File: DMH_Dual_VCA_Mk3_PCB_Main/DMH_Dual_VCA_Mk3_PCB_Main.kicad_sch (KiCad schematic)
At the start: 58 parts, among them J1 TRS_Jack_6.35mm_Sw, J10 IDC_02x05, J11 Conn_01x06, J12 Conn_01x08, J13 Conn_01x06, J14 Conn_01x06, J15 Conn_01x08, J16 Conn_01x06, J17 IDC_02x05, J18 Conn_02x03_Odd_Even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

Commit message: Schematic redesign done
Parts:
- J20, JP1: now in the parts list

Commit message: Controls PCB comp placement started
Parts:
- J12: footprint Connector_PinSocket_2.54mm:PinSocket_1x06_P2.54mm_Vertical -> Connector_PinSocket_2.54mm:PinSocket_1x08_P2.54mm_Vertical
- J15: footprint Connector_PinHeader_2.54mm:PinHeader_1x06_P2.54mm_Vertical -> Connector_PinHeader_2.54mm:PinHeader_1x08_P2.54mm_Vertical
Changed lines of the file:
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@@
 			)
 		)
-		(property "Footprint" "Connector_PinSocket_2.54mm:PinSocket_1x06_P2.54mm_Vertical"
+		(property "Footprint" "Connector_PinSocket_2.54mm:PinSocket_1x08_P2.54mm_Vertical"
 			(at 101.6 195.58 0)
 			(hide yes)
@@
 			(at 101.6 195.58 0)
 			(hide yes)
+			(show_name no)
+			(do_not_autoplace no)
+			(effects
+				(font
+					(size 1.27 1.27)
+				)
+			)
+		)
+		(property "Function" ""
+			(at 101.6 195.58 0)
 			(show_name no)
 			(do_not_autoplace no)
@@
 			)
 		)
-		(property "Footprint" "Connector_PinHeader_2.54mm:PinHeader_1x06_P2.54mm_Vertical"
+		(property "Footprint" "Connector_PinHeader_2.54mm:PinHeader_1x08_P2.54mm_Vertical"
 			(at 139.7 195.58 0)
 			(hide yes)
@@
 			(show_name no)
 			(do_not_autoplace no)
+			(effects
+				(font
+					(size 1.27 1.27)
+				)
+			)
+		)
+		(property "Function" ""
+			(at 139.7 195.58 0)
+			(show_name no)
+			(do_not_autoplace no)

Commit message: Started Main PCB comp placement
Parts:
- removed J21: Conn_01x04, Connector_PinHeader_2.54mm:PinHeader_1x04_P2.54mm_Vertical, symbol Connector_Generic:Conn_01x04
- removed J24: Conn_01x04, Connector_PinSocket_2.54mm:PinSocket_1x04_P2.54mm_Vertical, symbol Connector_Generic:Conn_01x04
- J11: footprint Connector_PinSocket_2.54mm:PinSocket_1x06_P2.54mm_Vertical -> Connector_PinHeader_2.54mm:PinHeader_1x06_P2.54mm_Vertical
- J12: footprint Connector_PinSocket_2.54mm:PinSocket_1x08_P2.54mm_Vertical -> Connector_PinHeader_2.54mm:PinHeader_1x08_P2.54mm_Vertical
- J14, J16: footprint Connector_PinHeader_2.54mm:PinHeader_1x06_P2.54mm_Vertical -> Connector_PinSocket_2.54mm:PinSocket_1x06_P2.54mm_Vertical
- J15: footprint Connector_PinHeader_2.54mm:PinHeader_1x08_P2.54mm_Vertical -> Connector_PinSocket_2.54mm:PinSocket_1x08_P2.54mm_Vertical
- J18, J19, J22, J23: footprint Connector_PinHeader_2.54mm:PinHeader_2x03_P2.54mm_Horizontal -> Connector_PinSocket_2.54mm:PinSocket_2x03_P2.54mm_Vertical
- J20: now left out of the parts list
- JP1: footprint (none) -> Connector_PinHeader_2.54mm:PinHeader_1x03_P2.54mm_Vertical; now left out of the parts list
- U4: footprint (none) -> Package_DIP:DIP-8_W7.62mm_Socket
- renumbered J17 to J100, J10 to J200
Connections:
- net +12V: now also J13.5 (Pin_5), J16.5 (Pin_5); no longer J13.2 (Pin_2), J16.2 (Pin_2)
- net +5V: now also J13.2 (Pin_2), J16.2 (Pin_2); no longer J13.4 (Pin_4), J16.4 (Pin_4)
- net -12V: now also J13.4 (Pin_4), J16.4 (Pin_4); no longer J13.3 (Pin_3), J16.3 (Pin_3)
- net -5V: now also J13.3 (Pin_3), J16.3 (Pin_3); no longer J13.5 (Pin_5), J16.5 (Pin_5)
- net Attenuverted_CV_PT_c: now also J15.4 (Pin_4); no longer J15.3 (Pin_3)
- net Attenuverted_CV_PT_m: now also J12.4 (Pin_4); no longer J12.3 (Pin_3)
- net Balanced_Offset_c: now also J15.6 (Pin_6); no longer J15.1 (Pin_1)
- net Balanced_Offset_m: now also J12.6 (Pin_6); no longer J12.1 (Pin_1)
- net CV_In_A2_N_m: now also J200.6 (Pin_6); no longer J200.4 (Pin_4)
- net CV_In_B2_N_m: now also J200.8 (Pin_8); no longer J200.6 (Pin_6)
- net CV_In_PT_c: now also J15.1 (Pin_1); no longer J15.8 (Pin_8)
- net CV_In_PT_m: now also J12.1 (Pin_1); no longer J12.8 (Pin_8)
- net CV_PT_Offset_c: now also J15.8 (Pin_8); no longer J15.5 (Pin_5)
- net CV_PT_Offset_m: now also J12.8 (Pin_8); no longer J12.5 (Pin_5)
- net CV_PT_Pot_G1_c: now also J15.3 (Pin_3); no longer J15.6 (Pin_6)
- net CV_PT_Pot_G1_m: now also J12.3 (Pin_3); no longer J12.6 (Pin_6)
- net CV_PT_Pot_G2_c: now also J15.2 (Pin_2); no longer J15.7 (Pin_7)
- net CV_PT_Pot_G2_m: now also J12.2 (Pin_2); no longer J12.7 (Pin_7)
- net Input_B_N_m: now also J200.2 (Pin_2); no longer J200.9 (Pin_9)
- net Inverted_CV_PT_c: now also J15.7 (Pin_7); no longer J15.2 (Pin_2)
- net Inverted_CV_PT_m: now also J12.7 (Pin_7); no longer J12.2 (Pin_2)
- net Output_A_N_m: now also J200.9 (Pin_9); no longer J200.2 (Pin_2)
- net Output_B_N_m: now also J200.4 (Pin_4); no longer J200.8 (Pin_8)
- net Processed_CV_PT_c: now also J15.5 (Pin_5); no longer J15.4 (Pin_4)
- net Processed_CV_PT_m: now also J12.5 (Pin_5); no longer J12.4 (Pin_4)

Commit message: Comp placement in progress
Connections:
- net CV_In_A1_N_m: now also J200.8 (Pin_8); no longer J200.3 (Pin_3)
- net CV_In_A2_N_m: now also J200.1 (Pin_1); no longer J200.6 (Pin_6)
- net CV_In_B2_N_m: now also J200.3 (Pin_3); no longer J200.8 (Pin_8)
- net Input_A_N_m: now also J200.6 (Pin_6); no longer J200.1 (Pin_1)
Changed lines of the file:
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@@
 	)
 	(label "Input_A_N_m"
-		(at 29.21 261.62 180)
+		(at 46.99 261.62 0)
 		(effects
 			(font
 				(size 1.27 1.27)
 			)
-			(justify right bottom)
+			(justify left bottom)
 		)
 	)
@@
 	)
 	(label "CV_In_A1_N_m"
-		(at 29.21 266.7 180)
+		(at 46.99 266.7 0)
 		(effects
 			(font
 				(size 1.27 1.27)
 			)
-			(justify right bottom)
+			(justify left bottom)
 		)
 	)
@@
 	)
 	(label "CV_In_B2_N_m"
-		(at 46.99 266.7 0)
+		(at 29.21 266.7 180)
 		(effects
 			(font
 				(size 1.27 1.27)
 			)
-			(justify left bottom)
+			(justify right bottom)
 		)
 	)
@@
 	)
 	(label "CV_In_A2_N_m"
-		(at 46.99 261.62 0)
+		(at 29.21 261.62 180)
 		(effects
 			(font
 				(size 1.27 1.27)
 			)
-			(justify left bottom)
+			(justify right bottom)
 		)
 	)

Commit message: Main comp placement in progress
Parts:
- U1, U2: footprint Package_TO_SOT_THT:TO-92_Inline -> Package_TO_SOT_THT:TO-92L_Inline_Wide
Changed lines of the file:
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@@
 			)
 		)
-		(property "Footprint" "Package_TO_SOT_THT:TO-92_Inline"
+		(property "Footprint" "Package_TO_SOT_THT:TO-92L_Inline_Wide"
 			(at 109.22 273.05 0)
 			(hide yes)
@@
 			(at 114.3 273.05 0)
 			(hide yes)
+			(show_name no)
+			(do_not_autoplace no)
+			(effects
+				(font
+					(size 1.27 1.27)
+				)
+			)
+		)
+		(property "Function" ""
+			(at 114.3 273.05 0)
 			(show_name no)
 			(do_not_autoplace no)
@@
 			)
 		)
-		(property "Footprint" "Package_TO_SOT_THT:TO-92_Inline"
+		(property "Footprint" "Package_TO_SOT_THT:TO-92L_Inline_Wide"
 			(at 147.32 273.05 0)
 			(hide yes)
@@
 			(show_name no)
 			(do_not_autoplace no)
+			(effects
+				(font
+					(size 1.27 1.27)
+				)
+			)
+		)
+		(property "Function" ""
+			(at 152.4 273.05 0)
+			(show_name no)
+			(do_not_autoplace no)

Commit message: Main comp placement done
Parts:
- J9: Function CV Pan/Tremolo -> CV P/T
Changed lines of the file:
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@@
 			)
 		)
-		(property "Function" "CV Pan/Tremolo"
+		(property "Function" "CV P/T"
 			(at 24.765 219.71 0)
 			(show_name no)

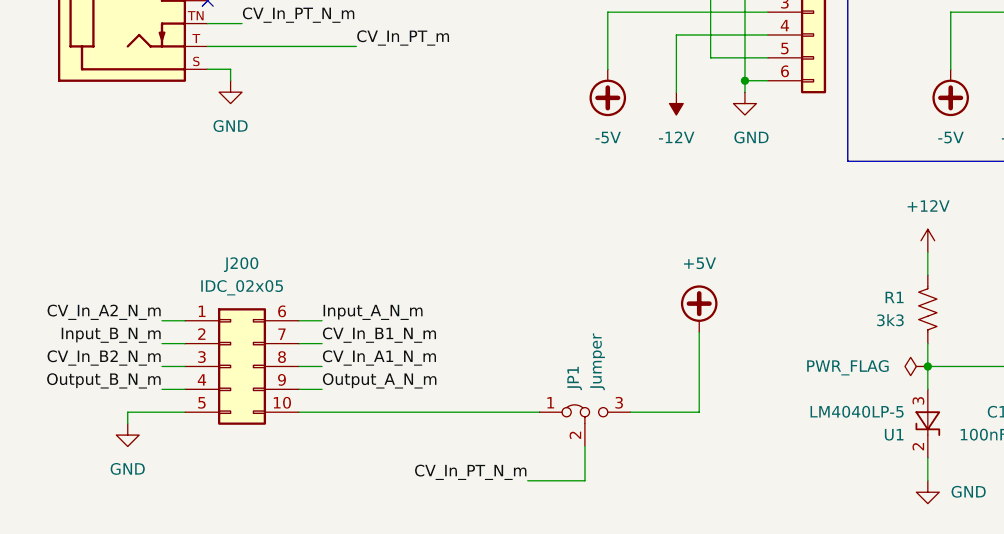
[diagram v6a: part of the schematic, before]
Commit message: Added jumpers to normalize CV inputs B to A
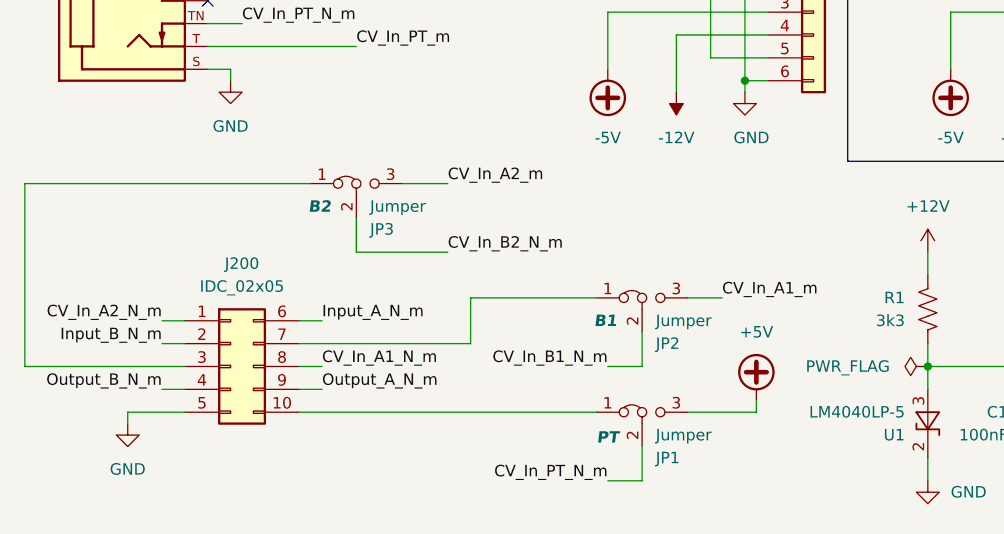
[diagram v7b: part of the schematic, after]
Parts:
- added JP2, JP3: Jumper, Connector_PinHeader_2.54mm:PinHeader_1x03_P2.54mm_Vertical, symbol Jumper:Jumper_3_Bridged12
- JP1: Function (none) -> PT; now in the parts list
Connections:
- net CV_In_A1_m: now also JP2.3 (B)
- net CV_In_A2_m: now also JP3.3 (B)
- net CV_In_B1_N_m: now also JP2.2 (C); no longer J200.7 (Pin_7)
- net CV_In_B2_N_m: now also JP3.2 (C); no longer J200.3 (Pin_3)
- new net: J200.7 (Pin_7), JP2.1 (A)
- new net: J200.3 (Pin_3), JP3.1 (A)
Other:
- moved on the sheet: JP1

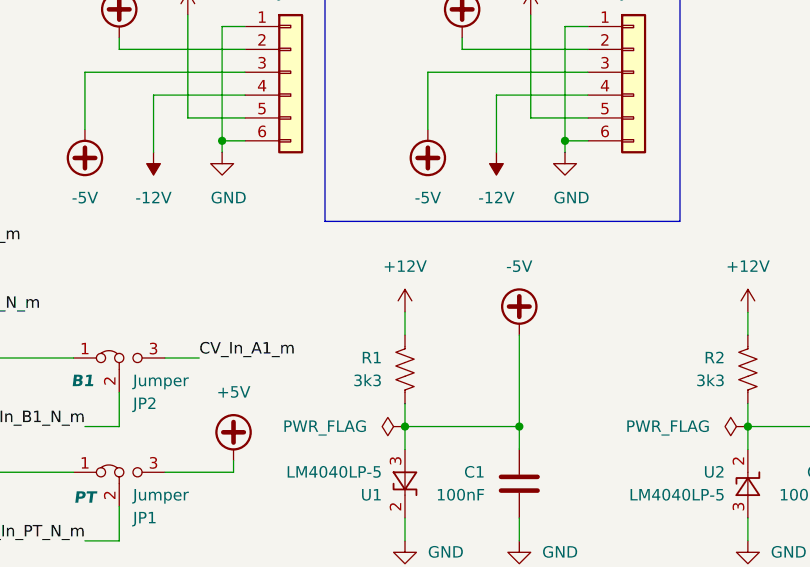
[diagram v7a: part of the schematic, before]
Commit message: Fixed -5V supply circuit mistake
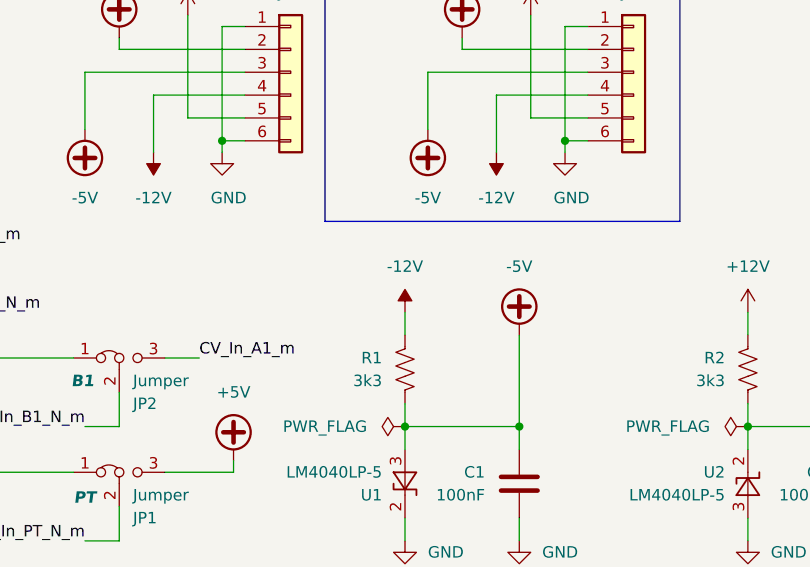
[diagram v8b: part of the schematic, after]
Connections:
- net +12V: no longer R1.2
- net -12V: now also R1.2
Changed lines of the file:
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@@
 	)
 	(symbol
-		(lib_id "power:+12V")
-		(at 114.3 254 0)
-		(unit 1)
-		(body_style 1)
-		(exclude_from_sim no)
-		(in_bom yes)
-		(on_board yes)
-		(in_pos_files yes)
-		(dnp no)
-		(fields_autoplaced yes)
-		(property "Reference" "#PWR017"
-			(at 114.3 257.81 0)
-			(hide yes)
-			(show_name no)
-			(do_not_autoplace no)
-			(effects
-				(font
-					(size 1.27 1.27)
-				)
-			)
-		)
-		(property "Value" "+12V"
-			(at 114.3 248.92 0)
-			(show_name no)
-			(do_not_autoplace no)
-			(effects
-				(font
-					(size 1.27 1.27)
-				)
-			)
-		)
-		(property "Footprint" ""
-			(at 114.3 254 0)
-			(hide yes)
-			(show_name no)
-			(do_not_autoplace no)
-			(effects
-				(font
-					(size 1.27 1.27)
-				)
-			)
-		)
-		(property "Datasheet" ""
-			(at 114.3 254 0)
-			(hide yes)
-			(show_name no)
-			(do_not_autoplace no)
-			(effects
-				(font
-					(size 1.27 1.27)
-				)
-			)
-		)
-		(property "Description" "Power symbol creates a global label with name \"+12V\""
-			(at 114.3 254 0)
-			(hide yes)
-			(show_name no)
-			(do_not_autoplace no)
-			(effects
-				(font
-					(size 1.27 1.27)
-				)
-			)
-		)
-		(pin "1"
-		)
-		(instances
-			(project "DMH_Dual_VCA_Mk3_PCB_Main"
-				(path "/58f4306d-5387-4983-bb08-41a2313fd315"
-					(reference "#PWR017")
-					(unit 1)
-				)
-			)
-		)
-	)
-	(symbol
 		(lib_id "power:+VDC")
 		(at 95.25 270.51 0)
@@
 					(unit 1)
 				)
+			)
+		)
+	)
+	(symbol
+		(lib_id "power:-12V")
+		(at 114.3 254 0)
+		(unit 1)
+		(body_style 1)
+		(exclude_from_sim no)
+		(in_bom yes)
+		(on_board yes)
+		(in_pos_files yes)
+		(dnp no)
+		(fields_autoplaced yes)
+		(property "Reference" "#PWR017"
+			(at 114.3 257.81 0)
+			(hide yes)
+			(show_name no)
+			(do_not_autoplace no)
+			(effects
+				(font
+					(size 1.27 1.27)
+				)
+			)
+		)
+		(property "Value" "-12V"
+			(at 114.3 248.92 0)
+			(show_name no)
+			(do_not_autoplace no)
+			(effects
+				(font
+					(size 1.27 1.27)
+				)
+			)
+		)
+		(property "Footprint" ""
+			(at 114.3 254 0)
+			(hide yes)
+			(show_name no)
+			(do_not_autoplace no)
+			(effects
+				(font
+					(size 1.27 1.27)
+				)
+			)
+		)
+		(property "Datasheet" ""
+			(at 114.3 254 0)
+			(hide yes)
+			(show_name no)
+			(do_not_autoplace no)
+			(effects
+				(font
+					(size 1.27 1.27)
+				)
+			)
+		)
+		(property "Description" "Power symbol creates a global label with name \"-12V\""
+			(at 114.3 254 0)
+			(hide yes)
+			(show_name no)
+			(do_not_autoplace no)
+			(effects
+				(font
+					(size 1.27 1.27)
+				)
+			)
+		)
+		(pin "1"
+		)
+		(instances
+			(project "DMH_Dual_VCA_Mk3_PCB_Main"
+				(path "/58f4306d-5387-4983-bb08-41a2313fd315"
+					(reference "#PWR017")
+					(unit 1)
+				)
